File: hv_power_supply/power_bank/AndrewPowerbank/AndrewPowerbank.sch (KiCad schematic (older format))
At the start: 49 parts, among them J1 NanoFit_RA_TH_02, J2 NanoFit_RA_TH_02, J3 USB-A-S-X-X-SM2, J4 USB-Micro-1981568-1, J5 NanoFit_RA_TH_02, Q1 SSM3K333R, U1 MCP73871T-2CCI_ML, U2 TPS61090RSAR

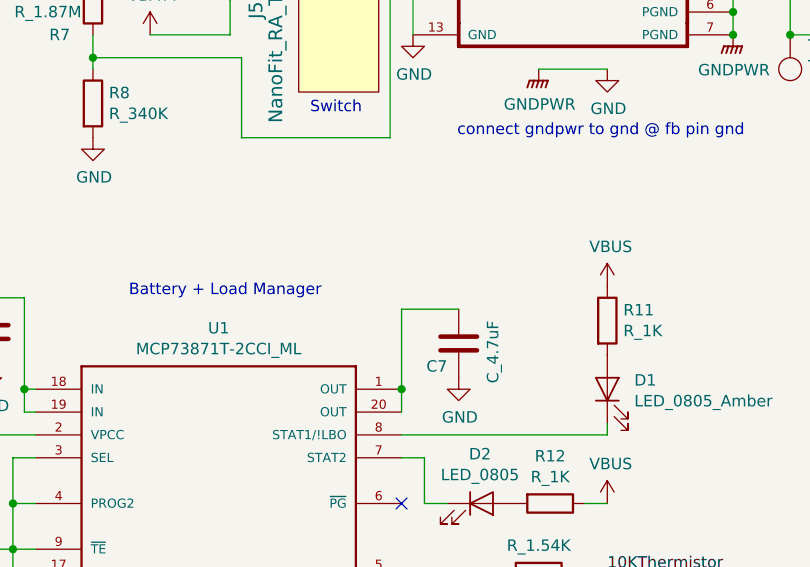
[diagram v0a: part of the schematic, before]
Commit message: Fix connection to C7.
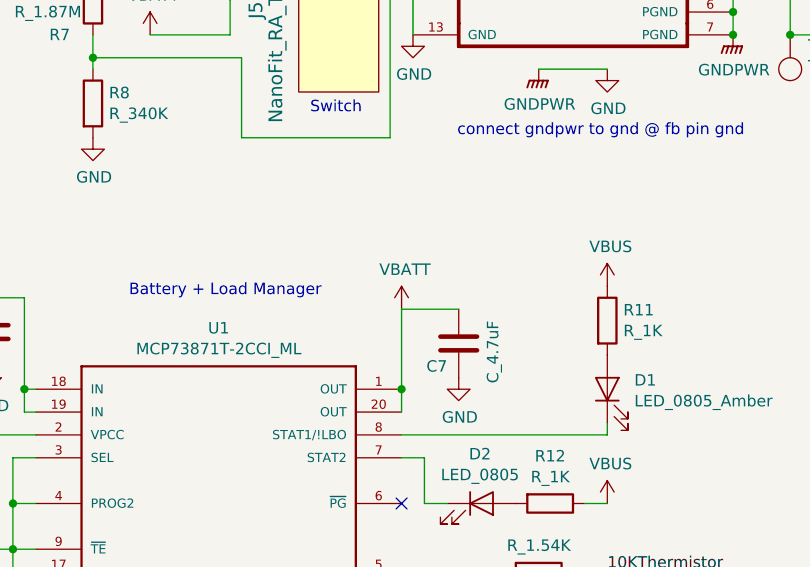
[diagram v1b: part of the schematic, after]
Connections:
- net +BATT: now also C7.1, U1.1 (OUT), U1.20 (OUT)
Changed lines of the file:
@@
 	5600 4550 5850 4550
 $Comp
-L power:GND #PWR?
+L power:GND #PWR0102
 U 1 1 607436CF
 P 5850 4850
-F 0 "#PWR?" H 5850 4600 50  0001 C CNN
+F 0 "#PWR0102" H 5850 4600 50  0001 C CNN
 F 1 "GND" H 5855 4677 50  0000 C CNN
 F 2 "" H 5850 4850 50  0001 C CNN
@@
 Wire Wire Line
 	5600 4550 5600 4900
+$Comp
+L formula:VBATT #PWR0103
+U 1 1 60755991
+P 5600 4550
+F 0 "#PWR0103" H 5600 4400 50  0001 C CNN
+F 1 "VBATT" H 5615 4723 50  0000 C CNN
+F 2 "" H 5600 4550 50  0001 C CNN
+F 3 "" H 5600 4550 50  0001 C CNN
+	1    5600 4550
+	1    0    0    -1
+$EndComp
 $EndSCHEMATC
